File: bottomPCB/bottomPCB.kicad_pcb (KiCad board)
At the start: 2 copper layers, 46 parts, among them J1 Conn_01x03_Pin, J2 Conn_02x03_Odd_Even, J3 Conn_01x02, J4 Conn_02x03_Odd_Even, J5 1-84953-1, J6 1-84953-1, J7 1-84953-1, J8 1-84953-1, U1 ESP32-WROOM-32, U2 XT30_horizontal, U8 LM1117IMPX-3_3_NOPB, U9 LM1117IMPX-3_3_NOPB

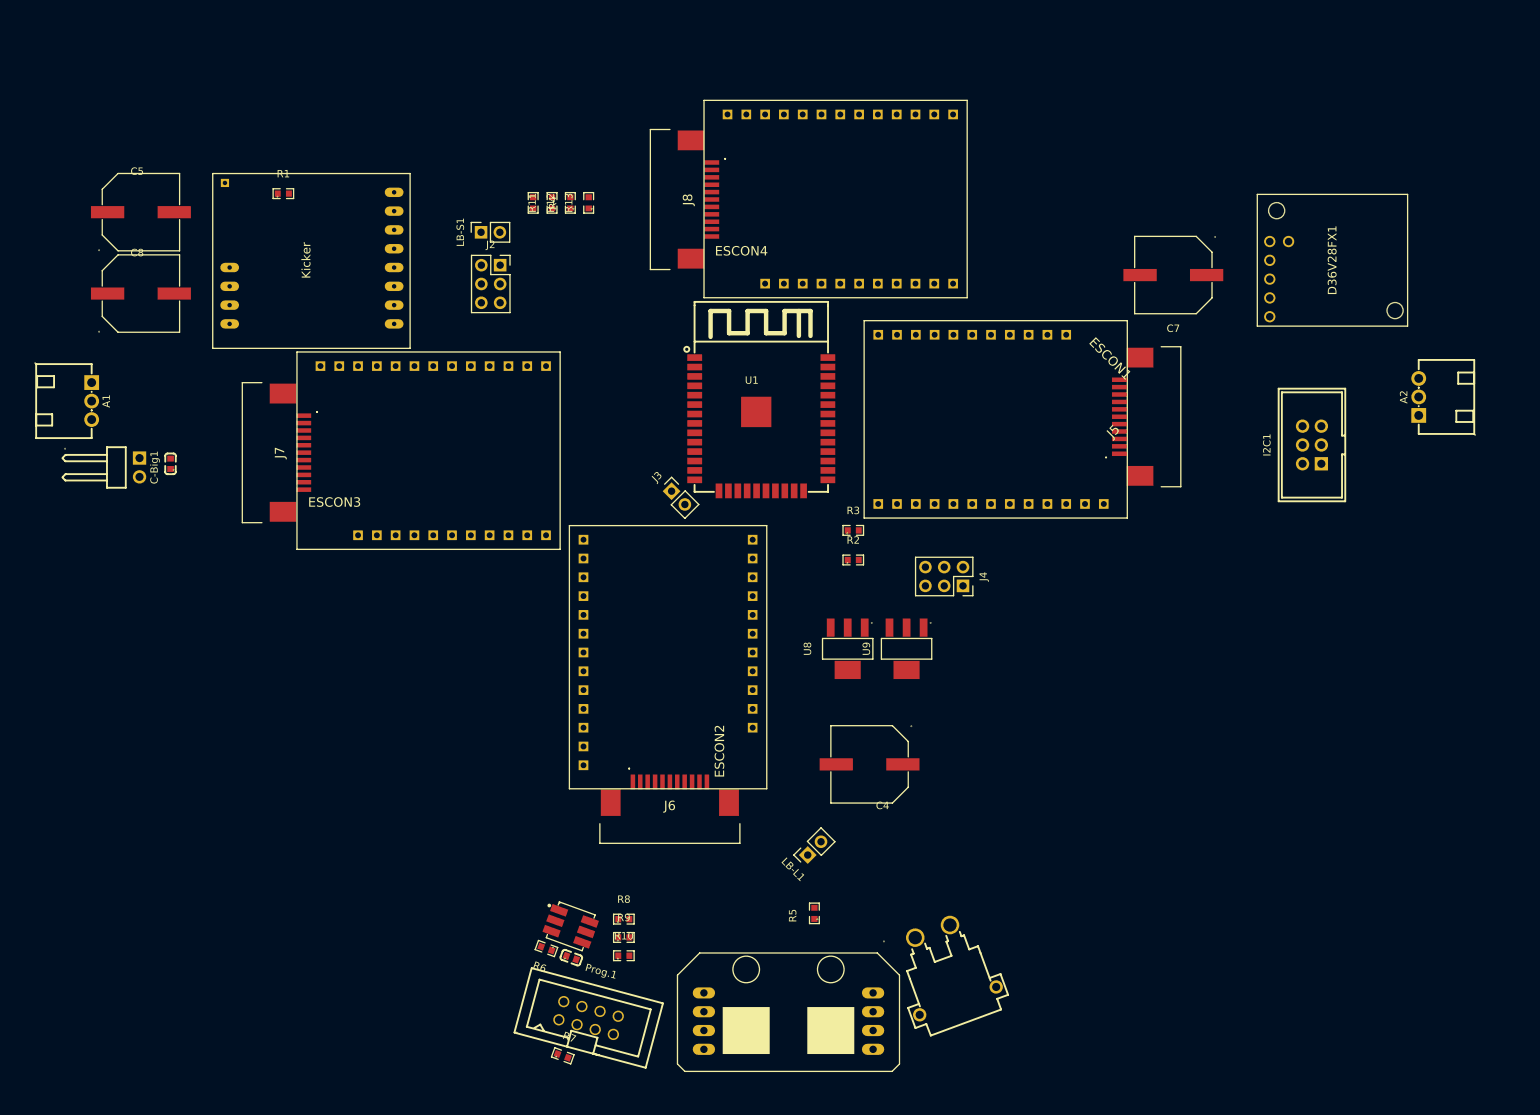
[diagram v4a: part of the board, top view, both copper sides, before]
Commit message: set edge cuts
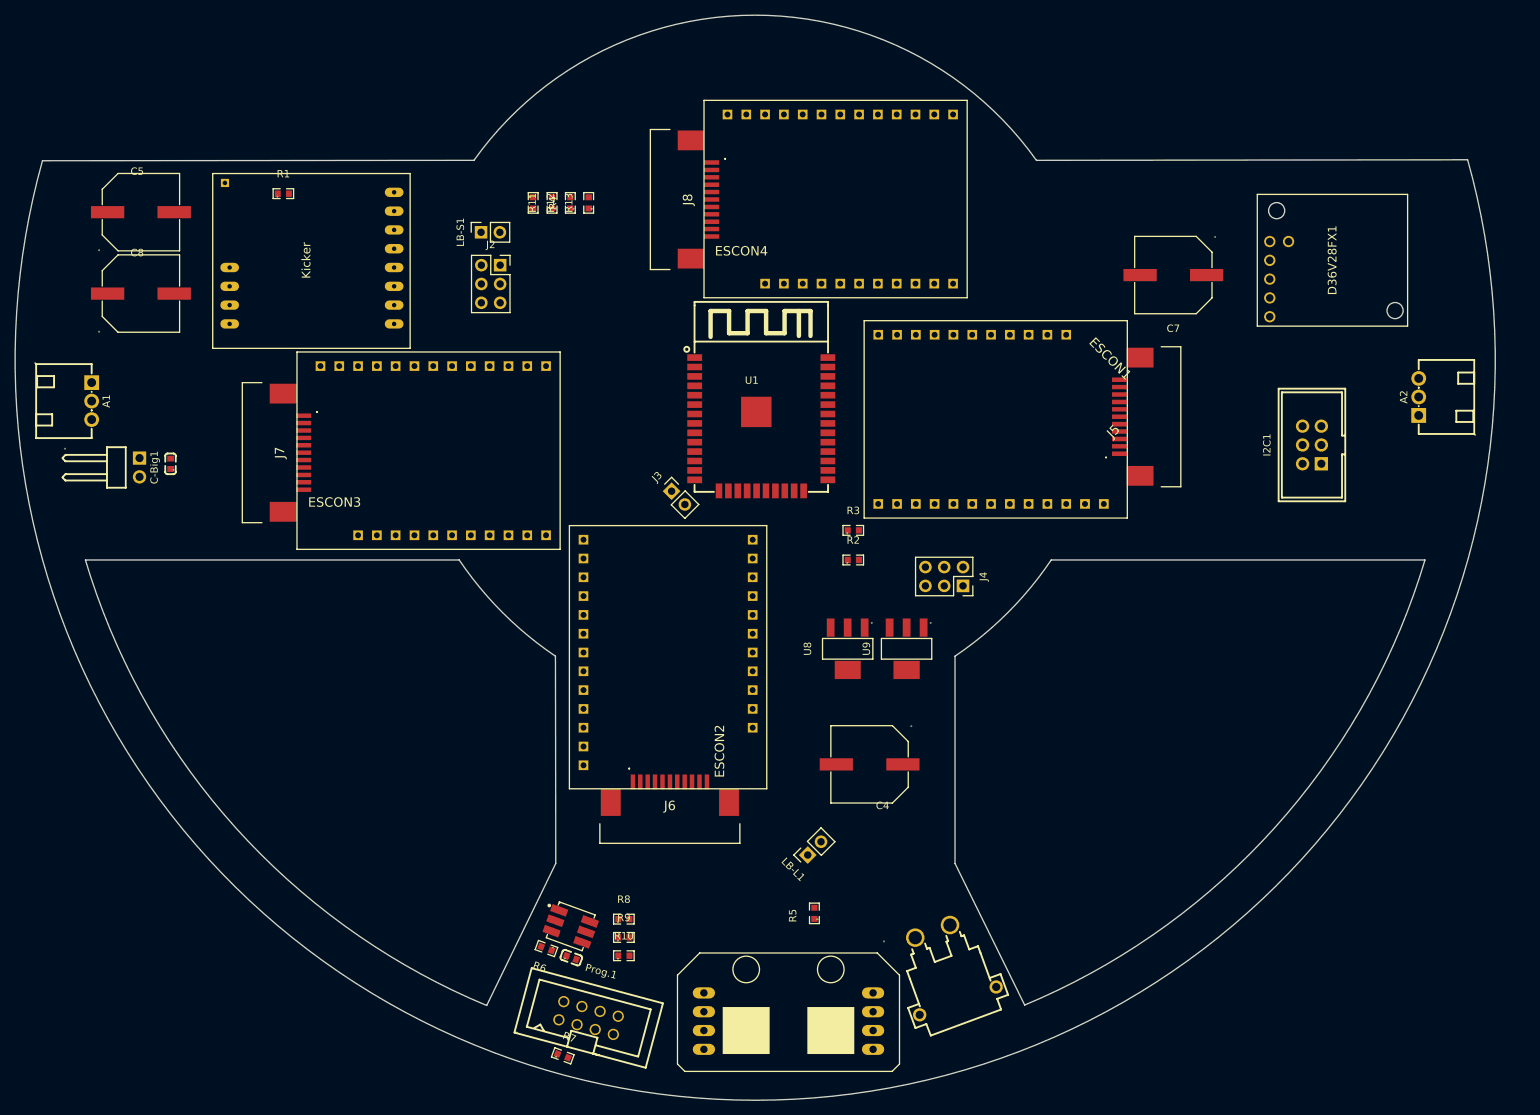
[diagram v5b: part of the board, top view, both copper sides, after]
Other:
- board outline added: 200 x 146.6 mm

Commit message: use edge cut polygons
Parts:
- moved A1 180.3 mm to (100.7, 12.0), turned to 90 degrees
- moved A2 180.3 mm to (-80.7, 11.5), turned to -90 degrees
- moved J1 45.3 mm to (238.0, 98.0)
- moved R7 23.2 mm to (-13.0, 81.0), turned to 160 degrees
- moved R12 0.25 mm to (-15.0, -11.0)
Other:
- outline, holes or cut-outs redrawn

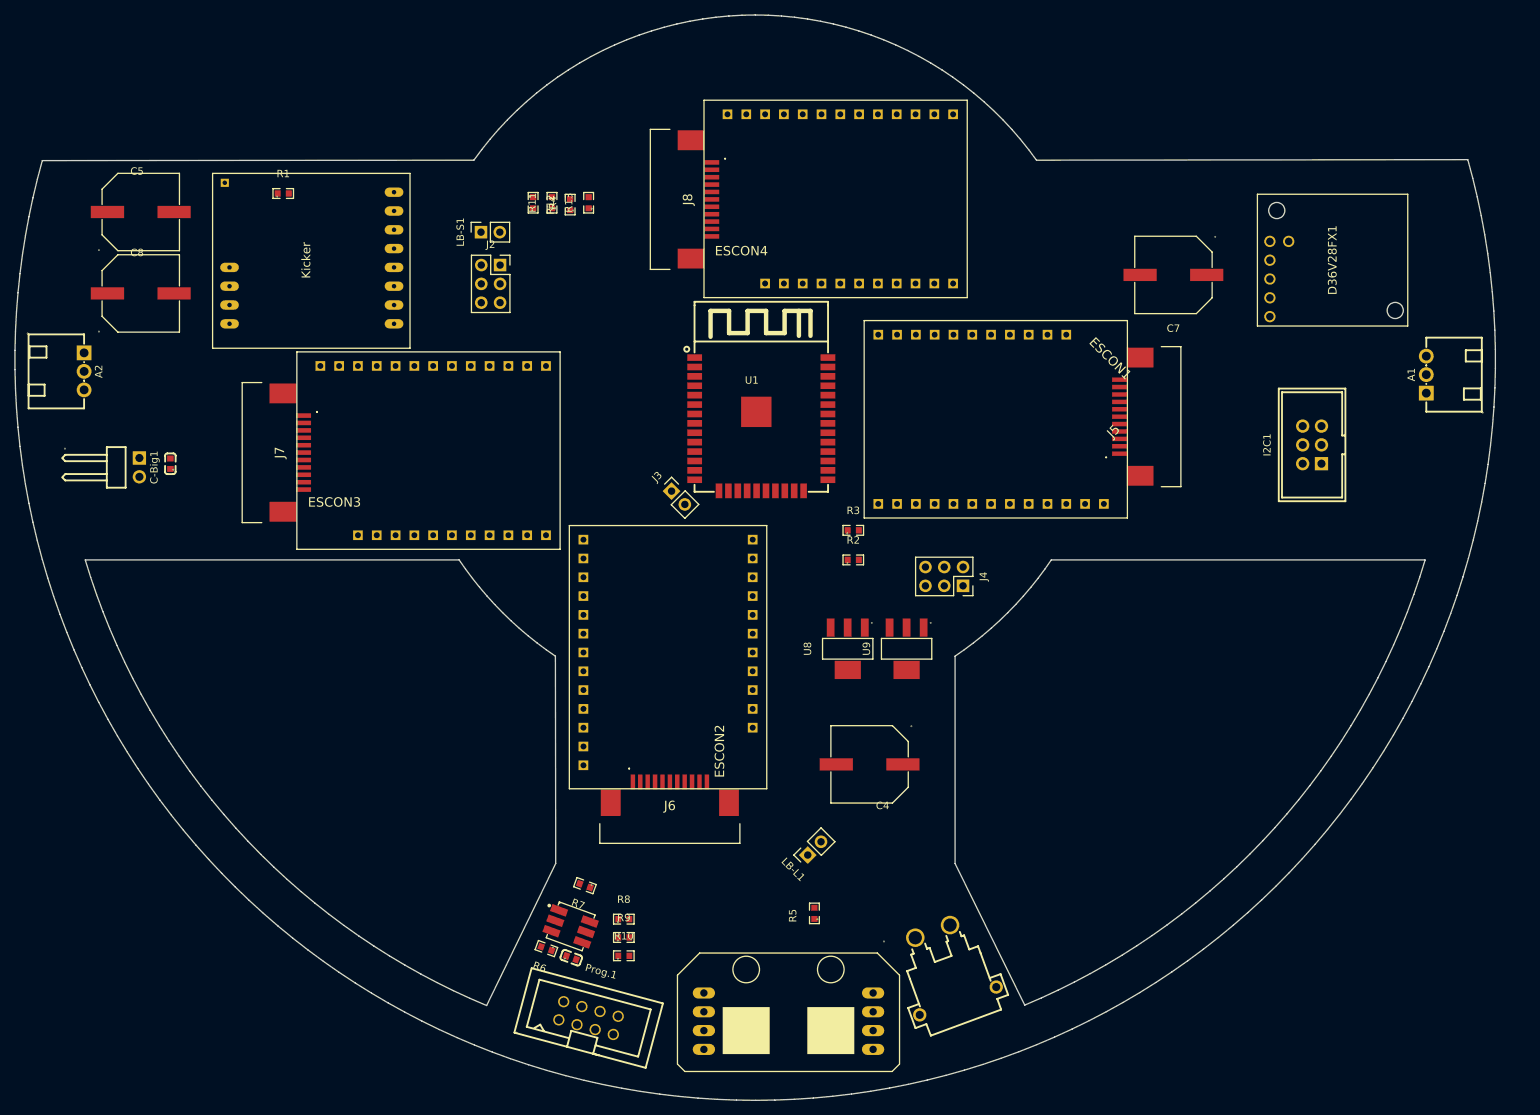
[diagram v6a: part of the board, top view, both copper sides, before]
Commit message: set edge cuts to octagon
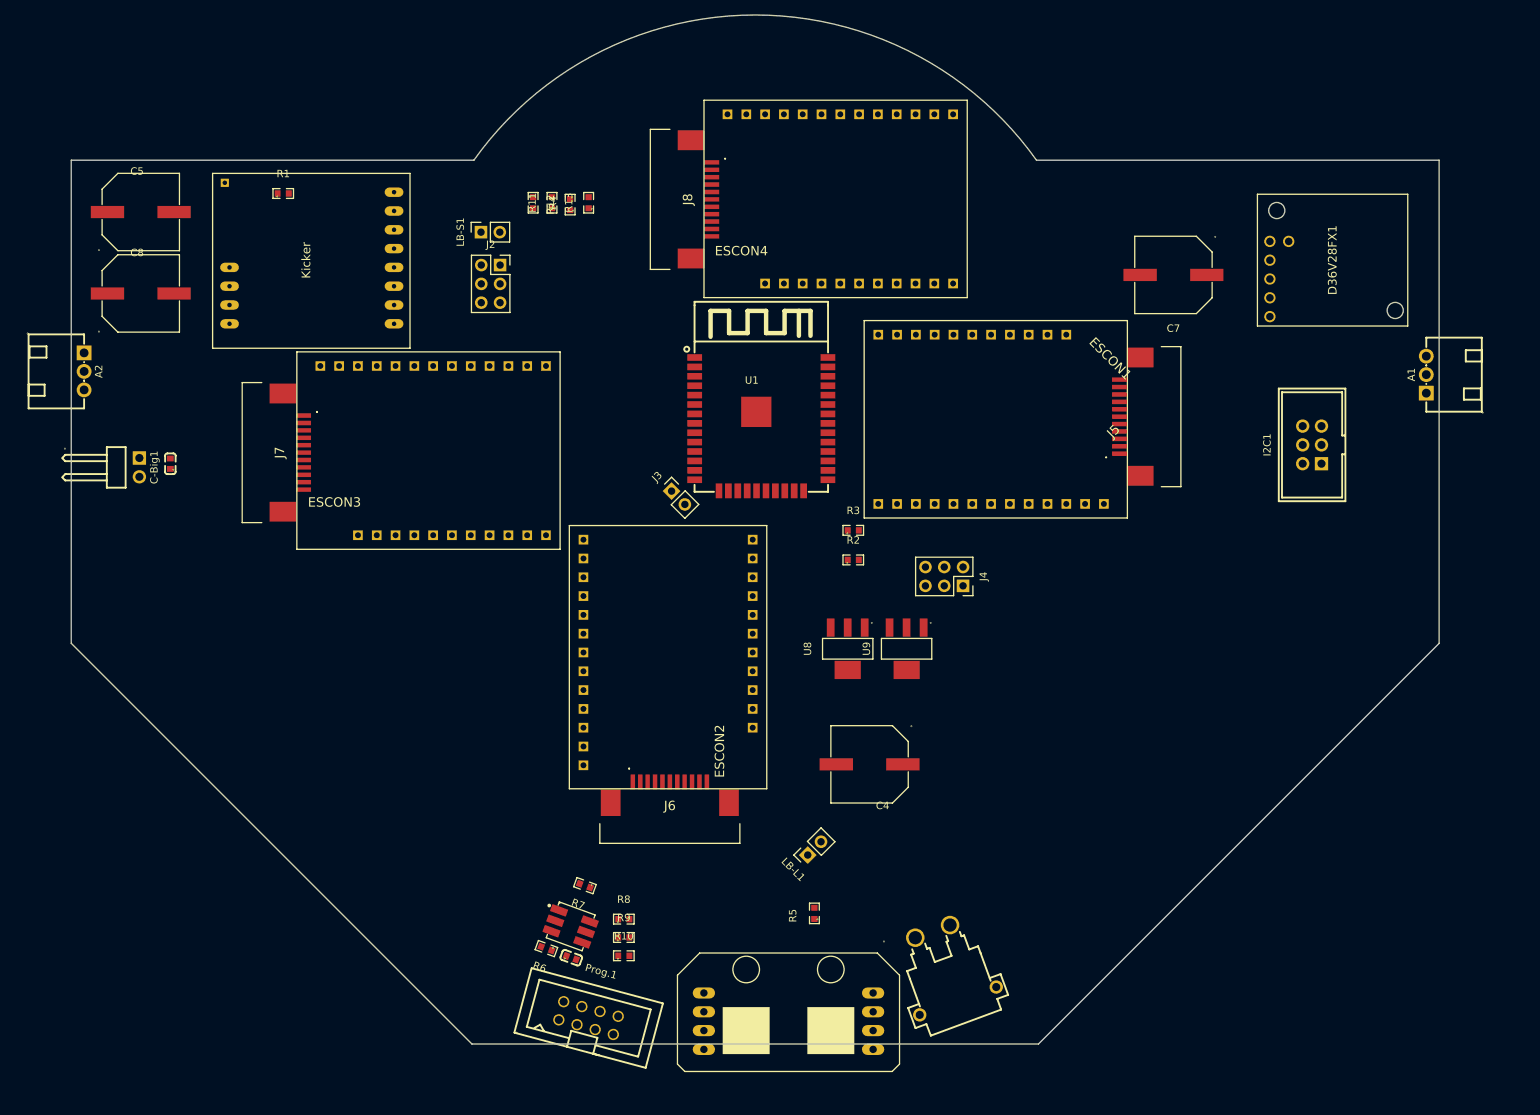
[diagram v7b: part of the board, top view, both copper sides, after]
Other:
- board size 200 x 146.6 mm -> 184.8 x 139 mm
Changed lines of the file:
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@@
 		(fp_arc
 			(start 1.390018 0.400203)
-			(mid 1.299267 0.619284)
+			(mid 1.299267 0.619281)
 			(end 1.080188 0.710033)
 			(stroke
@@
 		(tags "CONN-TH_XH-3AW-C722865 footprint")
 		(property "Reference" "A1"
-			(at 0 -2.000001 270)
+			(at 0 -2.000001 -90)
 			(layer "F.SilkS")
 			(effects
@@
 		)
 		(property "Value" "AKKU 1"
-			(at 0 9.499999 270)
+			(at 0 9.499999 -90)
 			(layer "F.Fab")
 			(effects
@@
 		)
 		(property "Footprint" "BohleBots:CONN-TH_XH-3AW-C722865"
-			(at 0 0 270)
+			(at 0 0 -90)
 			(layer "F.Fab")
 			(hide yes)
@@
 		)
 		(property "Datasheet" "https://item.szlcsc.com/767072.html?ref=editor&logined=true"
-			(at 0 0 270)
+			(at 0 0 -90)
 			(layer "F.Fab")
 			(hide yes)
@@
 		)
 		(property "Description" ""
-			(at 0 0 270)
+			(at 0 0 -90)
 			(layer "F.Fab")
 			(hide yes)
@@
 		)
 		(fp_text user "REF**"
-			(at 0 11.5 270)
+			(at 0 11.5 -90)
 			(layer "F.Fab")
 			(effects
@@
 		(fp_arc
 			(start 1.390018 0.400203)
-			(mid 1.299267 0.619284)
+			(mid 1.299267 0.61928)
 			(end 1.080188 0.710033)
 			(stroke
@@
 		)
 	)
-	(gr_poly
-		(pts
-			(arc
-				(start 37 50)
-				(mid 44.124771 44.124771)
-				(end 50 37)
-			)
-			(arc
-				(start 100.5 37)
-				(mid 80.22094 73.152749)
-				(end 46.414067 97.139347)
-			)
-			(xy 37 78)
+	(gr_line
+		(start 102.39 48.27)
+		(end 102.39 -17)
+		(stroke
+			(width 0.05)
+			(type default)
 		)
+		(layer "Edge.Cuts")
+	)
+	(gr_line
+		(start -28.27 102.39)
+		(end 48.27 102.39)
 		(stroke
 			(width 0.05)
-			(type solid)
+			(type default)
 		)
-		(fill none)
 		(layer "Edge.Cuts")
 	)
-	(gr_poly
-		(pts
-			(arc
-				(start 48 -17)
-				(mid 10 -36.615448)
-				(end -28 -17)
-			)
-			(arc
-				(start -86.301581 -16.944488)
-				(mid 10.067545 109.999952)
-				(end 106.265094 -17.074558)
-			)
+	(gr_line
+		(start -82.39 48.27)
+		(end -28.27 102.39)
+		(stroke
+			(width 0.05)
+			(type default)
 		)
+		(layer "Edge.Cuts")
+	)
+	(gr_arc
+		(start -28 -17)
+		(mid 10 -36.615448)
+		(end 48 -17)
 		(stroke
 			(width 0.05)
-			(type solid)
+			(type default)
 		)
-		(fill none)
 		(layer "Edge.Cuts")
 	)
-	(gr_poly
-		(pts
-			(arc
-				(start -29.994207 36.996091)
-				(mid -24.116159 44.1235)
-				(end -16.987485 50.000014)
-			)
-			(xy -16.944482 77.999983)
-			(arc
-				(start -26.278334 97.195942)
-				(mid -60.171743 73.207165)
-				(end -80.5 36.999617)
-			)
+	(gr_line
+		(start 48 -17)
+		(end 102.39 -17)
+		(stroke
+			(width 0.05)
+			(type default)
 		)
+		(layer "Edge.Cuts")
+	)
+	(gr_line
+		(start -82.39 48.27)
+		(end -82.39 -17)
 		(stroke
 			(width 0.05)
-			(type solid)
+			(type default)
+		)
+		(layer "Edge.Cuts")
+	)
+	(gr_line
+		(start -28 -17)
+		(end -82.39 -17)
+		(stroke
+			(width 0.05)
+			(type default)
+		)
+		(layer "Edge.Cuts")
+	)
+	(gr_line
+		(start 48.27 102.39)
+		(end 102.39 48.27)
+		(stroke
+			(width 0.05)
+			(type default)
 		)
-		(fill none)
 		(layer "Edge.Cuts")
 	)
@@
 		(layer "User.3")
 	)
-	(gr_rect
-		(start -17 37)
-		(end 37 109.5)
+	(gr_poly
+		(pts
+			(arc
+				(start 37 50)
+				(mid 44.124771 44.124771)
+				(end 50 37)
+			)
+			(arc
+				(start 100.5 37)
+				(mid 80.22094 73.152749)
+				(end 46.414067 97.139347)
+			)
+			(xy 37 78)
+		)
 		(stroke
-			(width 0.1)
-			(type default)
+			(width 0.05)
+			(type solid)
+		)
+		(fill none)
+		(layer "User.8")
+	)
+	(gr_poly
+		(pts
+			(arc
+				(start 48 -17)
+				(mid 10 -36.615448)
+				(end -28 -17)
+			)
+			(arc
+				(start -86.301581 -16.944488)
+				(mid 10.067545 109.999952)
+				(end 106.265094 -17.074558)
+			)
+		)
+		(stroke
+			(width 0.05)
+			(type solid)
+		)
+		(fill none)
+		(layer "User.8")
+	)
+	(gr_poly
+		(pts
+			(arc
+				(start -29.994207 36.996091)
+				(mid -24.116159 44.1235)
+				(end -16.987485 50.000014)
+			)
+			(xy -16.944482 77.999983)
+			(arc
+				(start -26.278334 97.195942)
+				(mid -60.171743 73.207165)
+				(end -80.5 36.999617)
+			)
+		)
+		(stroke
+			(width 0.05)
+			(type solid)
 		)
 		(fill none)
-		(layer "User.6")
+		(layer "User.8")
 	)
 	(gr_line
